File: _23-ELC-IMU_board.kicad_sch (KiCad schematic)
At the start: 10 parts, among them J1 MX150, J2 MX150, J3 Conn_01x03

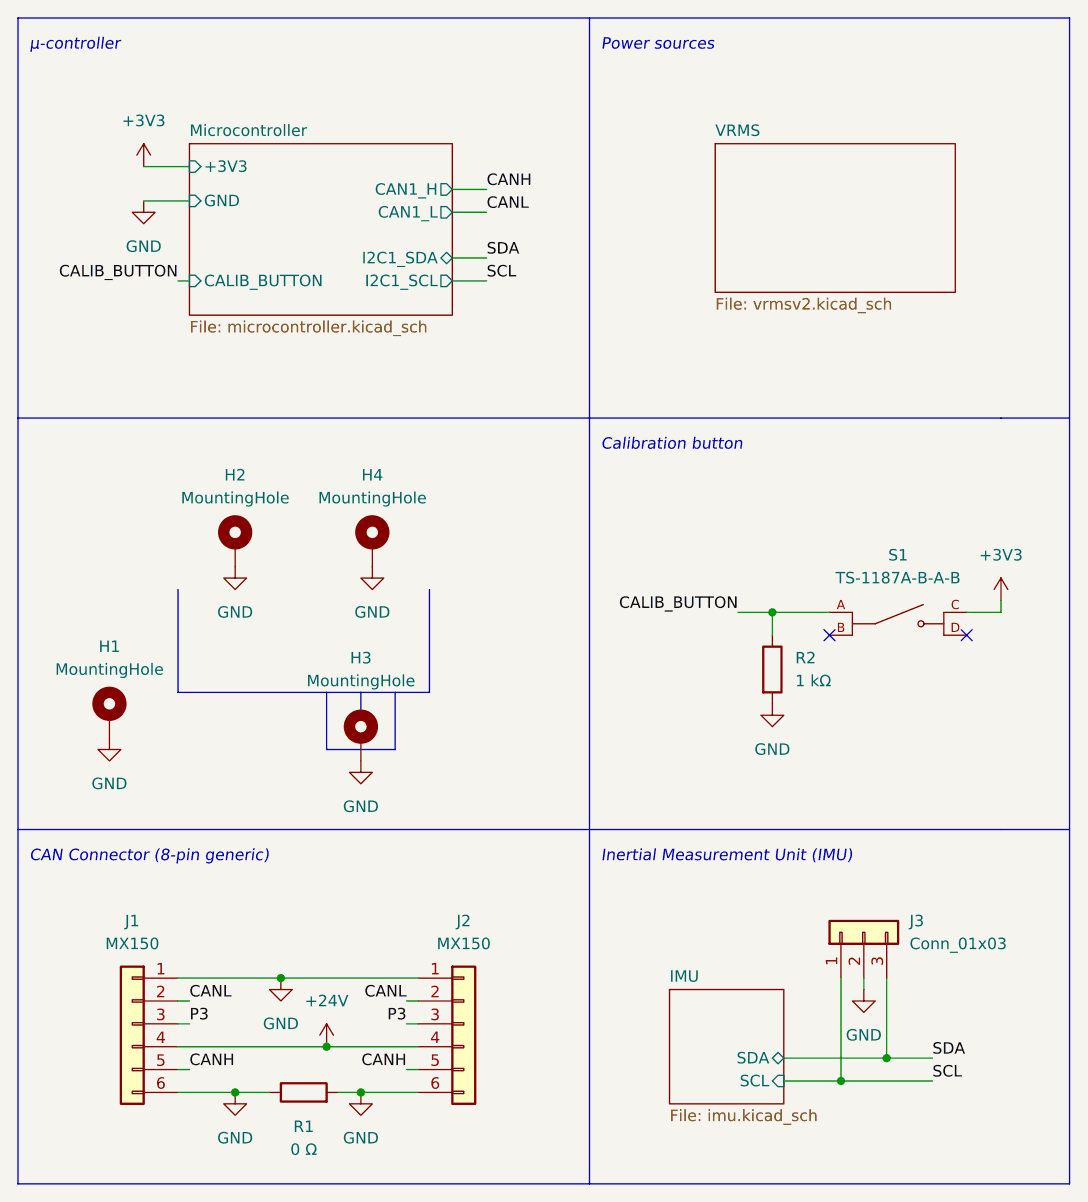
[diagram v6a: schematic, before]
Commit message: Added EEPROM chip for storing calibration data
Time to redo layout
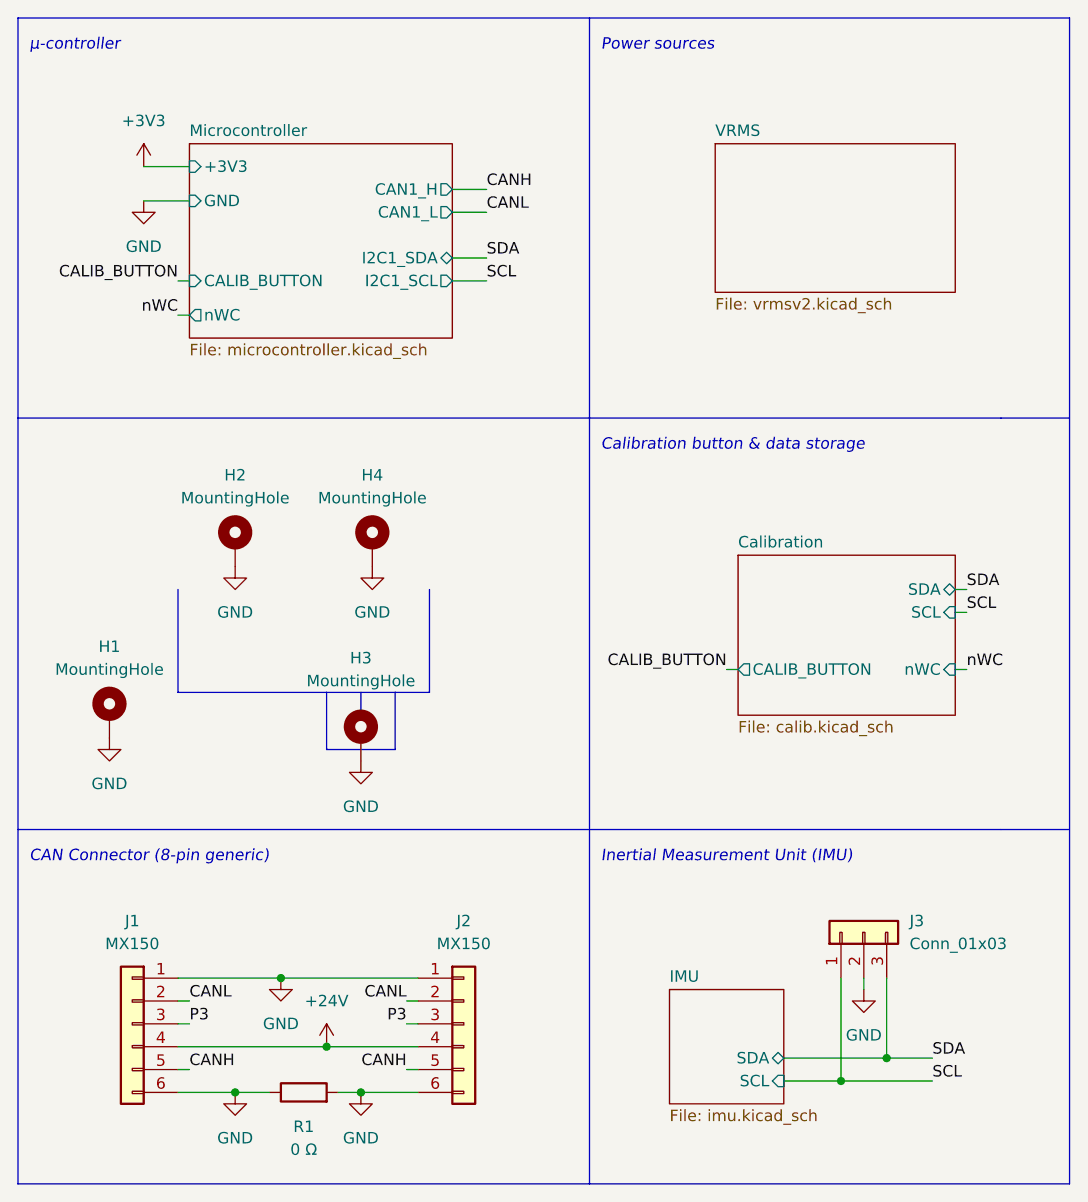
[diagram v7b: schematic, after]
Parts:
- removed R2: 1 kΩ, Resistor_SMD:R_0603_1608Metric_Pad0.98x0.95mm_HandSolder, symbol Device:R
- removed S1: TS-1187A-B-A-B, Push Buttons:SW_TS-1187A-B-A-B, symbol Push_Buttons:TS-1187A-B-A-B
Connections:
- no-connect marks 2 -> 0
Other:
- added sheet Calibration (calib.kicad_sch)
- sheet Microcontroller ports: added nWC; removed none
- note added: "Calibration button & data storage"
- note removed: "Calibration button"
